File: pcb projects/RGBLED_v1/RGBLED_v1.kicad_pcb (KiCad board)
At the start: 2 copper layers, 63 x 43 mm, 28 parts, among them CN1 USB_B_Micro, CN2 Conn_01x03_Pin, J1 Conn_02x02_Odd_Even, SW1 SW_MEC_5E, U1 STM32F091RBTx, U3 LM1117T-3.3, Y1 32.768kHz

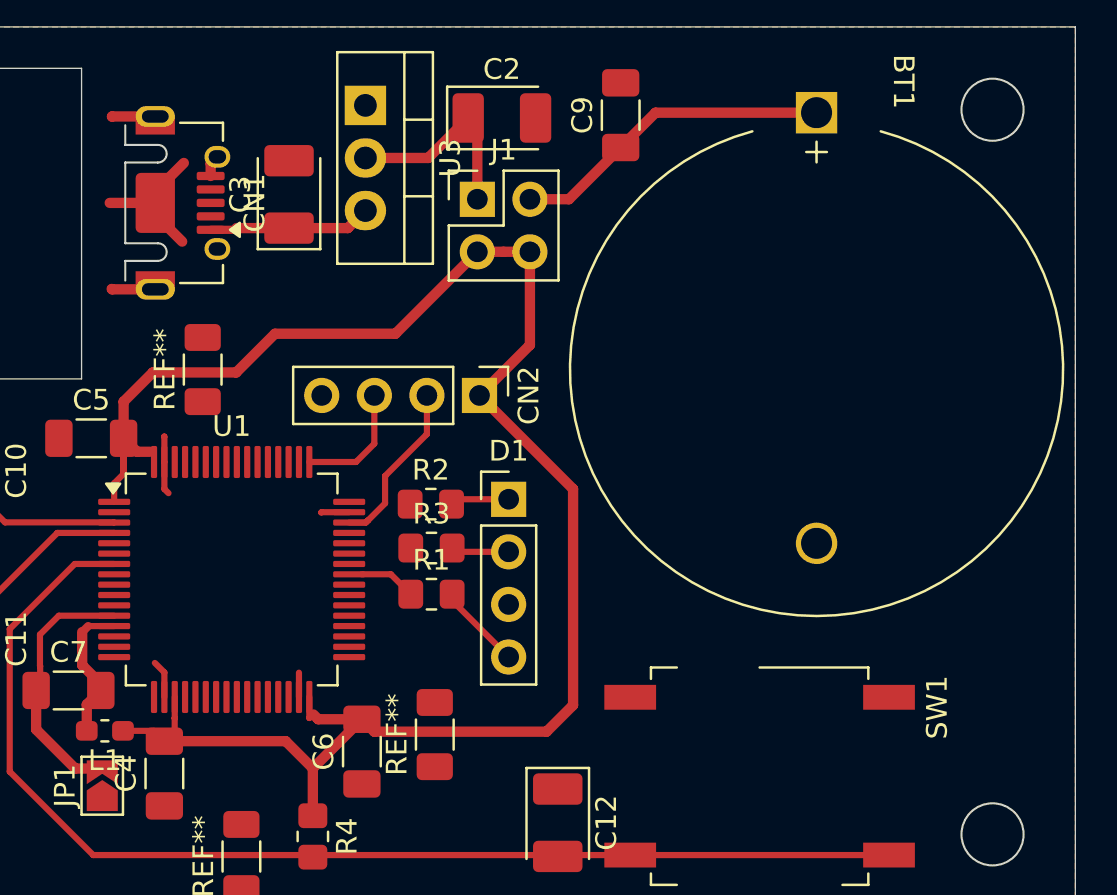
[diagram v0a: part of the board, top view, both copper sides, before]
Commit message: title added, D1 connected
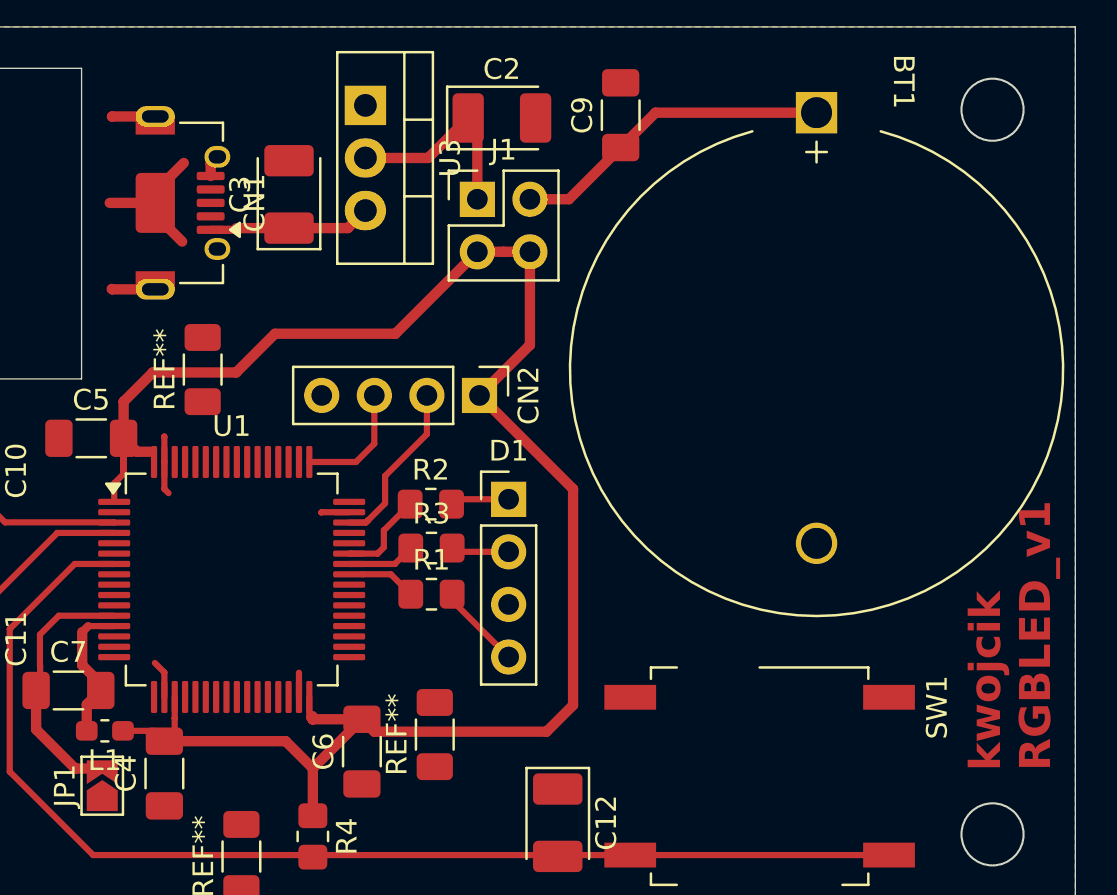
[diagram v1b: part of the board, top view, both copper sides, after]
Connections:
- R2 pad 1: Net-(U1-PA9) -> Net-(U1-PA10)
- R3 pad 1: Net-(U1-PA10) -> Net-(U1-PA9)
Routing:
- net Net-(U1-PA10): track 0.00 -> 4.42 mm
- net Net-(U1-PA9): track 0.00 -> 3.29 mm
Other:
- board text added: "kwojcik RGBLED_v1"

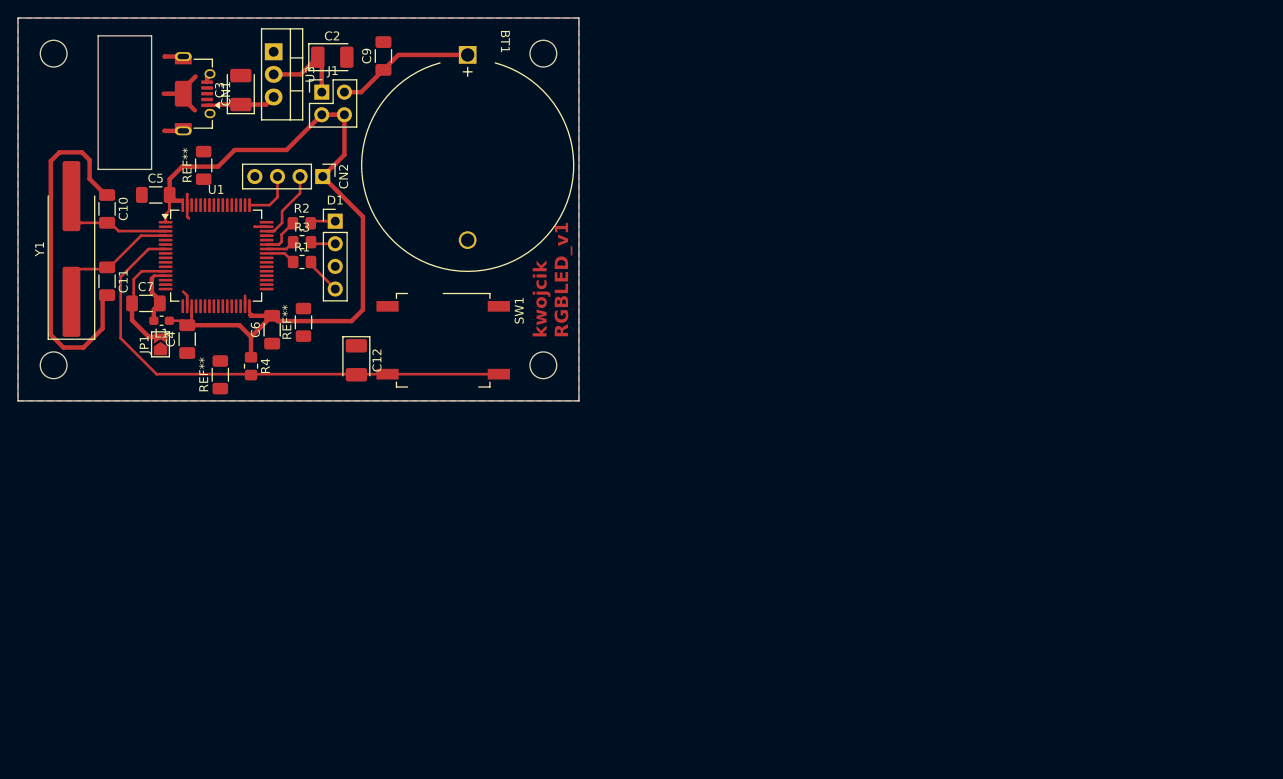
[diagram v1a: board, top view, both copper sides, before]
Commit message: and jumper changed, hanging zones cut
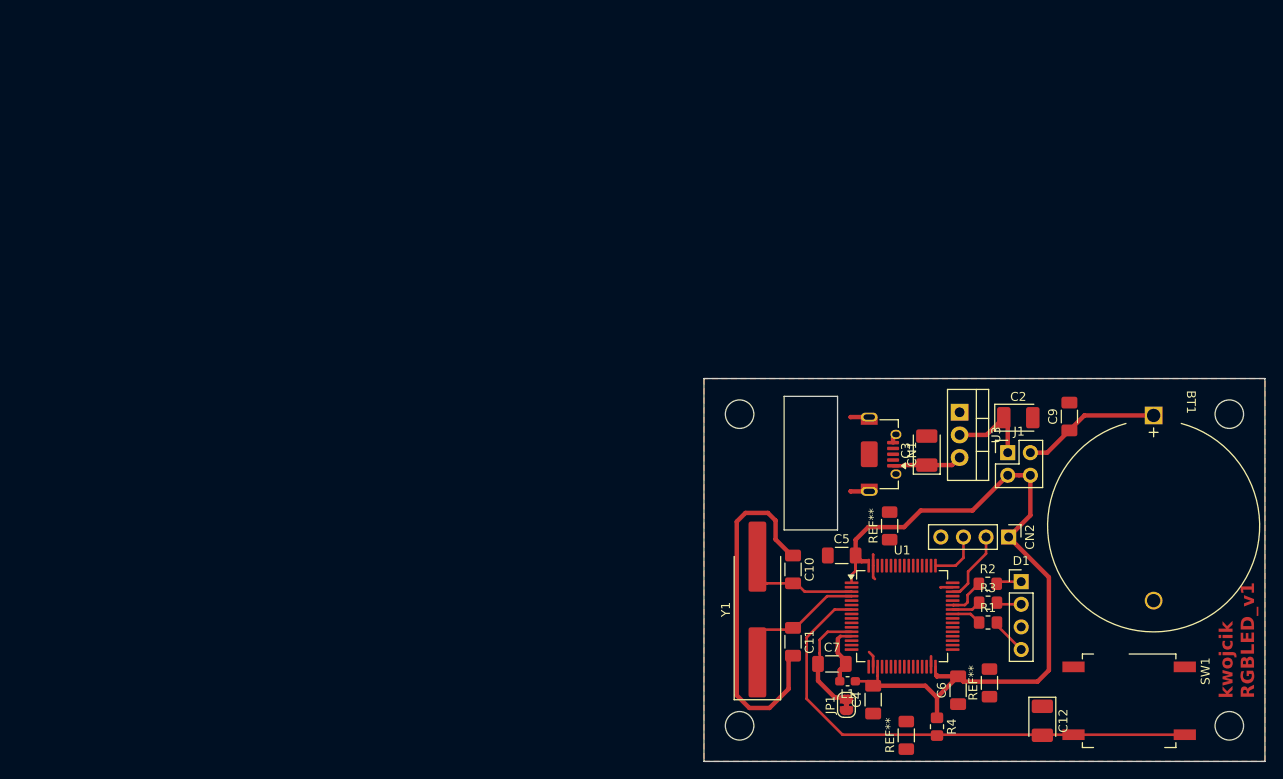
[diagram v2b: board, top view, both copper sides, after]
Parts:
- JP1: footprint Jumper:SolderJumper-2_P1.3mm_Open_TrianglePad1.0x1.5mm -> Jumper:SolderJumper-2_P1.3mm_Bridged_RoundedPad1.0x1.5mm
- moved BT1 87.0 mm to (96.0, 23.1)
- moved C10 87.0 mm to (55.5, 40.4)
- moved C11 87.0 mm to (55.5, 48.6)
- moved C12 87.0 mm to (83.5, 57.4)
- moved C2 87.0 mm to (80.8, 23.4)
- moved C3 87.0 mm to (70.6, 27.1)
- moved C4 87.0 mm to (64.5, 55.1)
- moved C5 87.0 mm to (61.0, 38.9)
- moved C6 87.0 mm to (74.1, 54.0)
- moved C9 87.0 mm to (86.6, 23.3)
- moved CN2 87.0 mm to (79.8, 36.8)
- moved D1 87.0 mm to (81.2, 41.8)
- moved J1 87.0 mm to (79.7, 27.3)
- moved JP1 87.0 mm to (61.5, 55.6)
- moved L1 87.0 mm to (61.7, 53.0)
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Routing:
- net GND: track 60.3 -> 54.3 mm
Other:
- outline, holes or cut-outs redrawn
